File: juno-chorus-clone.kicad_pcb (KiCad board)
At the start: 2 copper layers, 149.9 x 101.6 mm, 172 parts, among them P1 15VAC_IN, P2 AUDIO_IN, P3 AUDIO_OUT_1, P4 AUDIO_OUT_2, Q1 2SC1815, Q10 2SC1815, Q11 2SA1015, Q12 2SA1015, Q13 2SC1815, Q14 2SA1015, Q15 2SA1015, Q16 2SK30, Q17 2SK30, Q18 2SA1015, Q19 2SA1015, Q2 2SC1815, Q3 2SA1015, Q4 2SA1015, Q5 2SC1815, Q6 2SC1815, Q7 2SA1015, Q8 2SA1015, Q9 2SC1815, SW1 SW_PUSH, U1 TL082, U10 TL082, U2 LM7815CT, U3 LM7915CT, U4 TL082, U5 MN3009, U6 MN3101, U7 MN3009, U8 MN3101, U9 TL082

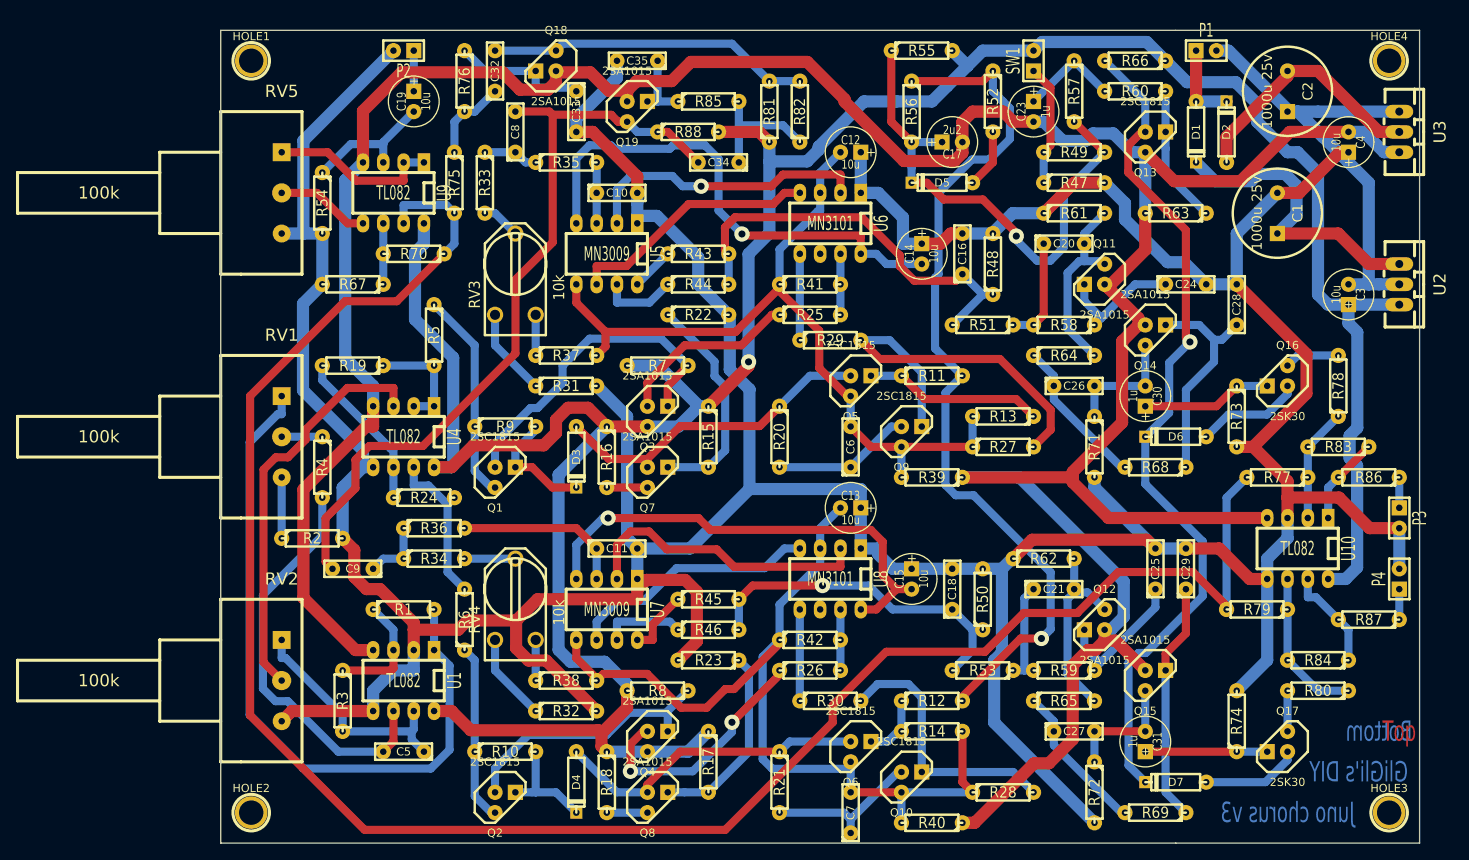
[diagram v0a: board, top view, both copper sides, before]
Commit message: Add ground plane to GliGli's through hole PCB
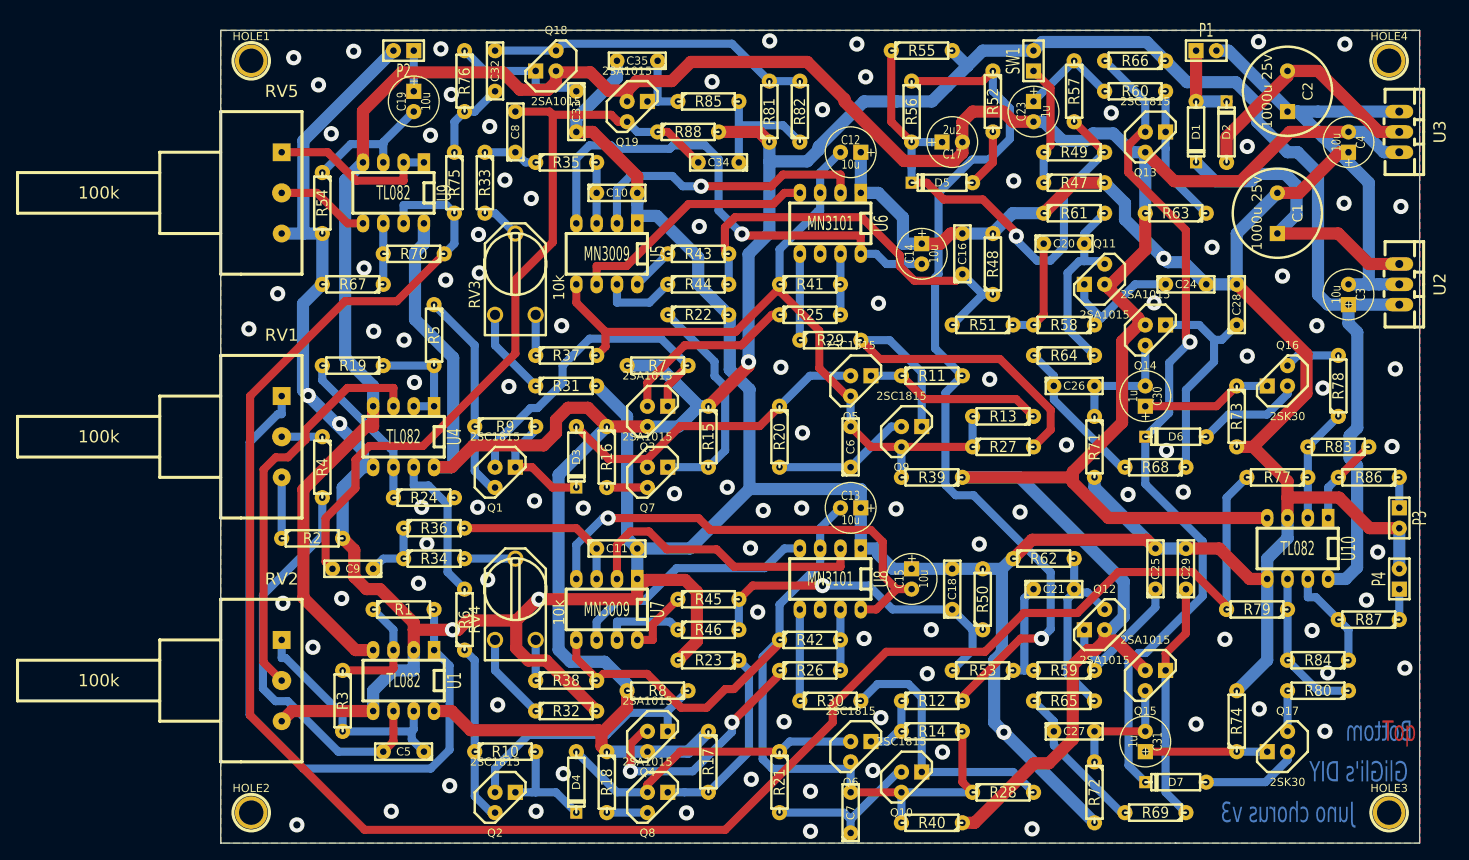
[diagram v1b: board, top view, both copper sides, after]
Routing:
- net GND: vias 0 -> 102
- added copper zone on B.Cu, net GND
- added copper zone on F.Cu, net GND
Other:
- net class Default removed
- net class pwr removed
